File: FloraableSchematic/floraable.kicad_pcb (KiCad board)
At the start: 2 copper layers, 27 parts, among them J1 USB_B, J2 soil moisture sensor, J3 water pump, Q1 IRL1404Z, Q2 IRL1404Z, U1 BA33BC0T, U2 BH1750, U3 NodeMCU, U4 TEM-HUM-AM2302(4P-25.0X15.0MM)

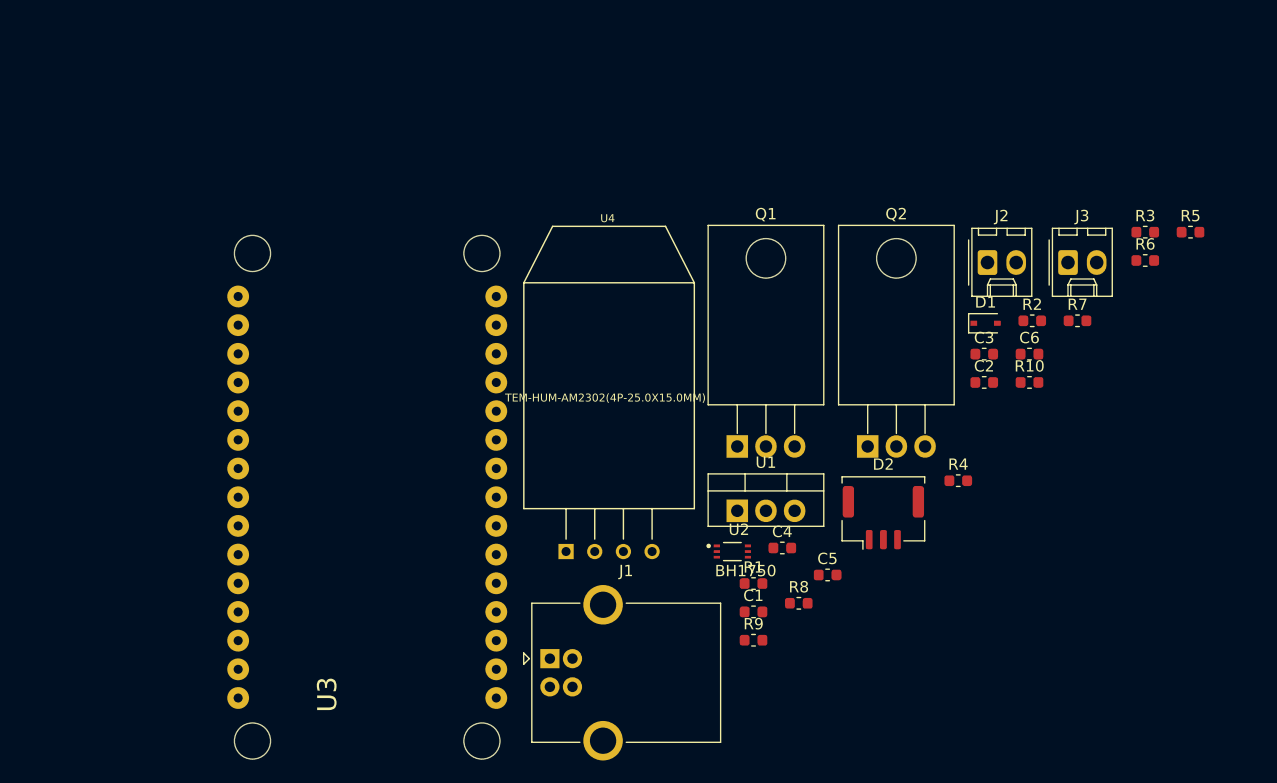
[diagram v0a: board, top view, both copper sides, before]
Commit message: check for existing devices
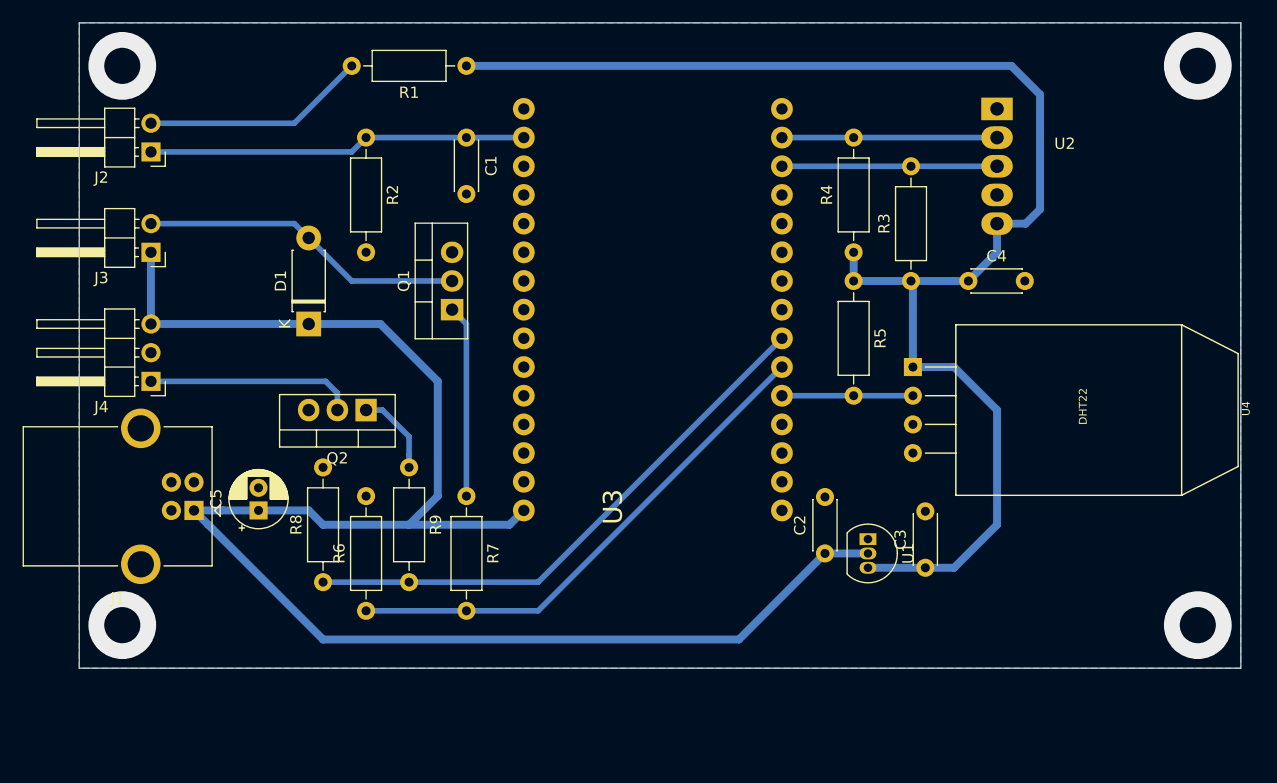
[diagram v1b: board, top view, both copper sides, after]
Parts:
- removed the C3 at (185.6, 94.1)
- removed D2: LED strip, Connector_Molex:Molex_CLIK-Mate_502382-0370_1x03-1MP_P1.25mm_Vertical
- removed the R3 at (199.8, 83.3)
- added J4: LED strip, Connector_PinHeader_2.54mm:PinHeader_1x03_P2.54mm_Horizontal, F.Cu at (111.8, 96.5)
- C1: footprint Capacitor_SMD:C_0603_1608Metric -> Capacitor_THT:C_Disc_D4.3mm_W1.9mm_P5.00mm
- C2: value 0.33u -> 1u; footprint Capacitor_SMD:C_0603_1608Metric -> Capacitor_THT:C_Disc_D4.3mm_W1.9mm_P5.00mm
- C3: renamed from C4; value 100u -> 1u; footprint Capacitor_SMD:C_0603_1608Metric -> Capacitor_THT:C_Disc_D4.3mm_W1.9mm_P5.00mm
- C4: renamed from C6; footprint Capacitor_SMD:C_0603_1608Metric -> Capacitor_THT:C_Disc_D4.3mm_W1.9mm_P5.00mm
- C5: value 100n -> 100u; footprint Capacitor_SMD:C_0603_1608Metric -> Capacitor_THT:CP_Radial_D5.0mm_P2.00mm
- D1: footprint Diode_SMD:D_SOD-323 -> Diode_THT:D_DO-41_SOD81_P7.62mm_Horizontal
- J2, J3: footprint Connector_Molex:Molex_KK-254_AE-6410-02A_1x02_P2.54mm_Vertical -> Connector_PinHeader_2.54mm:PinHeader_1x02_P2.54mm_Horizontal
- Q1, Q2: footprint Package_TO_SOT_THT:TO-220-3_Horizontal_TabDown -> Package_TO_SOT_THT:TO-220-3_Vertical
- R1, R2: footprint Resistor_SMD:R_0603_1608Metric -> Resistor_THT:R_Axial_DIN0207_L6.3mm_D2.5mm_P10.16mm_Horizontal
- R3: renamed from R4; footprint Resistor_SMD:R_0603_1608Metric -> Resistor_THT:R_Axial_DIN0207_L6.3mm_D2.5mm_P10.16mm_Horizontal
- R4: renamed from R5; footprint Resistor_SMD:R_0603_1608Metric -> Resistor_THT:R_Axial_DIN0207_L6.3mm_D2.5mm_P10.16mm_Horizontal
- R5: renamed from R6; footprint Resistor_SMD:R_0603_1608Metric -> Resistor_THT:R_Axial_DIN0207_L6.3mm_D2.5mm_P10.16mm_Horizontal
- R6: renamed from R7; footprint Resistor_SMD:R_0603_1608Metric -> Resistor_THT:R_Axial_DIN0207_L6.3mm_D2.5mm_P10.16mm_Horizontal
- R7: renamed from R8; footprint Resistor_SMD:R_0603_1608Metric -> Resistor_THT:R_Axial_DIN0207_L6.3mm_D2.5mm_P10.16mm_Horizontal
- R8: renamed from R9; footprint Resistor_SMD:R_0603_1608Metric -> Resistor_THT:R_Axial_DIN0207_L6.3mm_D2.5mm_P10.16mm_Horizontal
- R9: renamed from R10; footprint Resistor_SMD:R_0603_1608Metric -> Resistor_THT:R_Axial_DIN0207_L6.3mm_D2.5mm_P10.16mm_Horizontal
- U1: value BA33BC0T -> MCP1702-3302E/TO; footprint Package_TO_SOT_THT:TO-220-3_Vertical -> Package_TO_SOT_THT:TO-92_Inline
- U2: value BH1750 -> BH1750_module; footprint BH1750FVI-TR:XDCR_BH1750FVI-TR -> floraable:BH1750_module
- U3: footprint ESP12E_DEVKIT:ESP12E_DEVKIT -> floraable:newNodeMCU
- U4: value TEM-HUM-AM2302(4P-25.0X15.0MM) -> DHT22
- moved J3 81.2 mm to (111.8, 85.1), turned to 180 degrees
- moved J2 74.7 mm to (111.8, 76.2), turned to 180 degrees
- moved R6 68.0 mm to (130.8, 116.8), turned to 90 degrees
- moved R2 61.2 mm to (130.8, 74.9), turned to 270 degrees
- moved D1 59.9 mm to (125.7, 91.4), turned to 90 degrees
- moved R9 55.5 mm to (134.6, 104.1), turned to 270 degrees
- moved R1 52.4 mm to (139.7, 68.6), turned to 180 degrees
- moved C5 50.7 mm to (121.3, 108.0), turned to 90 degrees
- moved C1 49.1 mm to (139.7, 74.9), turned to 270 degrees
- moved Q2 44.5 mm to (130.8, 99.1), turned to 180 degrees
- moved U2 41.4 mm to (186.7, 77.5)
- moved U4 40.7 mm to (193.0, 99.1), turned to 270 degrees
- moved R8 38.5 mm to (127.0, 114.3), turned to 90 degrees
- moved J1 34.1 mm to (115.6, 108.0), turned to 180 degrees
- moved R7 30.9 mm to (139.7, 106.7), turned to 270 degrees
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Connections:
- C5 pad 1: Net-(C5-Pad1) -> +5V
- J2 pad 1: Net-(J2-Pad1) -> SOIL
- J2 pad 2: SOIL -> Net-(J2-Pad2)
- R1 pad 2: Net-(J2-Pad1) -> Net-(J2-Pad2)
- U1 pad 1: +5V -> GND
- U1 pad 2: GND -> +5V
- U2 pad 1: +3V3 -> Net-(U2-Pad1)
- U2 pad 2: Net-(U2-Pad2) -> SDA
- U2 pad 3: GND -> SCL
- U2 pad 4: SDA -> GND
- U2 pad 5: Net-(C5-Pad1) -> +3V3
- U3 pad D3: TEMPERATURE -> Net-(U3-PadD3)
- U3 pad D8: Net-(U3-PadD8) -> TEMPERATURE
- U3 pad GND@0: Net-(U3-PadGND@0) -> GND
- U3 pad GND@2: Net-(U3-PadGND@2) -> GND
- U3 pad GND@3: Net-(U3-PadGND@3) -> GND
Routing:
- net +5V: track 0.00 -> 145.4 mm
- net +3V3: track 0.00 -> 125.1 mm
- net LEDSTRIP: track 0.00 -> 49.6 mm
- net PUMP: track 0.00 -> 45.8 mm
- net SOIL: track 0.00 -> 33.5 mm
- net Net-(D1-Pad2): track 0.00 -> 28.8 mm
- net Net-(J2-Pad2): track 0.00 -> 19.9 mm
- net SDA: track 0.00 -> 19.1 mm
- net SCL: track 0.00 -> 19.1 mm
- net Net-(J4-Pad1): track 0.00 -> 18.4 mm
- net Net-(Q1-Pad1): track 0.00 -> 17.0 mm
- net TEMPERATURE: track 0.00 -> 11.6 mm
- net Net-(Q2-Pad1): track 0.00 -> 7.51 mm
- net (no net): vias 0 -> 4
- added copper zone on B.Cu, net GND
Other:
- board outline added: 102.9 x 57.2 mm
- rule trace_min: 0.2 -> 0.254
- rule via_min_size: 0.4 -> 0.508

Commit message: Add files via upload
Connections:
- U3 pad D5: Net-(U3-PadD5) -> TEMPERATURE
- U3 pad D8: TEMPERATURE -> Net-(U3-PadD8)
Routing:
- net TEMPERATURE: track 11.6 -> 17.0 mm
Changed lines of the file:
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@@
     (thickness 1.6)
     (drawings 6)
-    (tracks 69)
+    (tracks 71)
     (zones 0)
     (modules 25)
@@
     (40 Dwgs.User user)
     (41 Cmts.User user)
-    (42 Eco1.User user)
+    (42 Eco1.User user hide)
     (43 Eco2.User user)
     (44 Edge.Cuts user)
@@
   )
   (setup
-    (last_trace_width 0.7)
+    (last_trace_width 0.25)
     (user_trace_width 0.3)
     (user_trace_width 0.5)
@@
   (net 29 "Net-(U3-PadD4)")
   (net 30 "Net-(U3-Pad3V3@1)")
-  (net 31 "Net-(U3-PadD5)")
-  (net 32 PUMP)
-  (net 33 "Net-(U3-PadRX)")
-  (net 34 "Net-(U3-PadTX)")
-  (net 35 "Net-(U3-Pad3V3@2)")
-  (net 36 "Net-(U4-PadP$3)")
-  (net 37 "Net-(J2-Pad2)")
-  (net 38 "Net-(J4-Pad1)")
+  (net 31 PUMP)
+  (net 32 "Net-(U3-PadRX)")
+  (net 33 "Net-(U3-PadTX)")
+  (net 34 "Net-(U3-Pad3V3@2)")
+  (net 35 "Net-(U4-PadP$3)")
+  (net 36 "Net-(J2-Pad2)")
+  (net 37 "Net-(J4-Pad1)")
+  (net 38 "Net-(U3-PadD8)")
   (net_class Default "This is the default net class."
     (clearance 0.2)
@@
     (add_net "Net-(U3-PadD3)")
     (add_net "Net-(U3-PadD4)")
-    (add_net "Net-(U3-PadD5)")
+    (add_net "Net-(U3-PadD8)")
     (add_net "Net-(U3-PadEN)")
     (add_net "Net-(U3-PadRST)")
@@
     (fp_line (start -12.7 24.13) (end -12.7 -24.13) (layer F.Fab) (width 0.2032))
     (pad 3V3@2 thru_hole circle (at 11.43 17.78) (size 1.9304 1.9304) (drill 1) (layers *.Cu *.Mask)
-      (net 35 "Net-(U3-Pad3V3@2)") (solder_mask_margin 0.1016))
+      (net 34 "Net-(U3-Pad3V3@2)") (solder_mask_margin 0.1016))
     (pad GND@3 thru_hole circle (at 11.43 15.24) (size 1.9304 1.9304) (drill 1) (layers *.Cu *.Mask)
       (net 2 GND) (solder_mask_margin 0.1016))
     (pad TX thru_hole circle (at 11.43 12.7) (size 1.9304 1.9304) (drill 1) (layers *.Cu *.Mask)
-      (net 34 "Net-(U3-PadTX)") (solder_mask_margin 0.1016))
+      (net 33 "Net-(U3-PadTX)") (solder_mask_margin 0.1016))
     (pad RX thru_hole circle (at 11.43 10.16) (size 1.9304 1.9304) (drill 1) (layers *.Cu *.Mask)
-      (net 33 "Net-(U3-PadRX)") (solder_mask_margin 0.1016))
+      (net 32 "Net-(U3-PadRX)") (solder_mask_margin 0.1016))
     (pad D8 thru_hole circle (at 11.43 7.62) (size 1.9304 1.9304) (drill 1) (layers *.Cu *.Mask)
-      (net 10 TEMPERATURE) (solder_mask_margin 0.1016))
+      (net 38 "Net-(U3-PadD8)") (solder_mask_margin 0.1016))
     (pad D7 thru_hole circle (at 11.43 5.08) (size 1.9304 1.9304) (drill 1) (layers *.Cu *.Mask)
-      (net 32 PUMP) (solder_mask_margin 0.1016))
+      (net 31 PUMP) (solder_mask_margin 0.1016))
     (pad D6 thru_hole circle (at 11.43 2.54) (size 1.9304 1.9304) (drill 1) (layers *.Cu *.Mask)
       (net 11 LEDSTRIP) (solder_mask_margin 0.1016))
     (pad D5 thru_hole circle (at 11.43 0) (size 1.9304 1.9304) (drill 1) (layers *.Cu *.Mask)
-      (net 31 "Net-(U3-PadD5)") (solder_mask_margin 0.1016))
+      (net 10 TEMPERATURE) (solder_mask_margin 0.1016))
     (pad GND@2 thru_hole circle (at 11.43 -2.54) (size 1.9304 1.9304) (drill 1) (layers *.Cu *.Mask)
       (net 2 GND) (solder_mask_margin 0.1016))
@@
       (net 2 GND))
     (pad 2 thru_hole oval (at 2.54 0 180) (size 1.905 2) (drill 1.1) (layers *.Cu *.Mask)
-      (net 38 "Net-(J4-Pad1)"))
+      (net 37 "Net-(J4-Pad1)"))
     (pad 1 thru_hole rect (at 0 0 180) (size 1.905 2) (drill 1.1) (layers *.Cu *.Mask)
       (net 7 "Net-(Q2-Pad1)"))
@@
     (fp_line (start 1.93 -1.25) (end 1.93 1.25) (layer F.Fab) (width 0.1))
     (pad 2 thru_hole oval (at 10.16 0 270) (size 1.6 1.6) (drill 0.8) (layers *.Cu *.Mask)
-      (net 32 PUMP))
+      (net 31 PUMP))
     (pad 1 thru_hole circle (at 0 0 270) (size 1.6 1.6) (drill 0.8) (layers *.Cu *.Mask)
       (net 6 "Net-(Q1-Pad1)"))
@@
       (net 2 GND))
     (pad 1 thru_hole circle (at 0 0 90) (size 1.6 1.6) (drill 0.8) (layers *.Cu *.Mask)
-      (net 32 PUMP))
+      (net 31 PUMP))
     (model ${KISYS3DMOD}/Resistor_THT.3dshapes/R_Axial_DIN0207_L6.3mm_D2.5mm_P10.16mm_Horizontal.wrl
       (at (xyz 0 0 0))
@@
     (fp_line (start 1.93 -1.25) (end 1.93 1.25) (layer F.Fab) (width 0.1))
     (pad 2 thru_hole oval (at 10.16 0 180) (size 1.6 1.6) (drill 0.8) (layers *.Cu *.Mask)
-      (net 37 "Net-(J2-Pad2)"))
+      (net 36 "Net-(J2-Pad2)"))
     (pad 1 thru_hole circle (at 0 0 180) (size 1.6 1.6) (drill 0.8) (layers *.Cu *.Mask)
       (net 4 +3V3))
@@
     (fp_line (start 2.135 -1.27) (end 4.04 -1.27) (layer F.Fab) (width 0.1))
     (pad 2 thru_hole oval (at 0 2.54 180) (size 1.7 1.7) (drill 1) (layers *.Cu *.Mask)
-      (net 37 "Net-(J2-Pad2)"))
+      (net 36 "Net-(J2-Pad2)"))
     (pad 1 thru_hole rect (at 0 0 180) (size 1.7 1.7) (drill 1) (layers *.Cu *.Mask)
       (net 1 SOIL))
@@
       (net 2 GND))
     (pad P$3 thru_hole circle (at 1.27 13.8 270) (size 1.6 1.6) (drill 0.8) (layers *.Cu *.Mask)
-      (net 36 "Net-(U4-PadP$3)"))
+      (net 35 "Net-(U4-PadP$3)"))
     (pad P$2 thru_hole circle (at -1.27 13.8 270) (size 1.6 1.6) (drill 0.8) (layers *.Cu *.Mask)
       (net 10 TEMPERATURE))
@@
       (net 14 "Net-(J4-Pad2)"))
     (pad 1 thru_hole rect (at 0 0 180) (size 1.7 1.7) (drill 1) (layers *.Cu *.Mask)
-      (net 38 "Net-(J4-Pad1)"))
+      (net 37 "Net-(J4-Pad1)"))
     (model "D:/folder 0/download/KiCad/lib/DS1070-RA (WF-RA CONNFLY)/DS1070-3MR (WF-3RA CONNFLY).stp"
       (at (xyz 0 0 0))
@@
   (segment (start 173.99 74.93) (end 167.64 74.93) (width 0.5) (layer B.Cu) (net 9))
   (segment (start 179.24 97.79) (end 173.99 97.79) (width 0.5) (layer B.Cu) (net 10))
-  (segment (start 173.99 97.79) (end 167.64 97.79) (width 0.5) (layer B.Cu) (net 10))
+  (segment (start 170.18 90.17) (end 167.64 90.17) (width 0.5) (layer B.Cu) (net 10))
+  (segment (start 173.99 97.79) (end 173.99 93.98) (width 0.5) (layer B.Cu) (net 10))
+  (segment (start 173.99 93.98) (end 170.18 90.17) (width 0.5) (layer B.Cu) (net 10))
   (segment (start 146.05 114.3) (end 167.64 92.71) (width 0.5) (layer B.Cu) (net 11))
   (segment (start 134.62 114.3) (end 146.05 114.3) (width 0.5) (layer B.Cu) (net 11))
   (segment (start 127 114.3) (end 134.62 114.3) (width 0.5) (layer B.Cu) (net 11))
-  (segment (start 139.7 116.84) (end 146.05 116.84) (width 0.5) (layer B.Cu) (net 32))
-  (segment (start 146.05 116.84) (end 167.64 95.25) (width 0.5) (layer B.Cu) (net 32))
-  (segment (start 130.81 116.84) (end 139.7 116.84) (width 0.5) (layer B.Cu) (net 32))
-  (segment (start 124.46 73.66) (end 129.54 68.58) (width 0.5) (layer B.Cu) (net 37))
-  (segment (start 111.76 73.66) (end 124.46 73.66) (width 0.5) (layer B.Cu) (net 37))
-  (segment (start 128.27 97.56) (end 128.27 99.06) (width 0.5) (layer B.Cu) (net 38))
-  (segment (start 111.76 96.52) (end 127.23 96.52) (width 0.5) (layer B.Cu) (net 38))
-  (segment (start 127.23 96.52) (end 128.27 97.56) (width 0.5) (layer B.Cu) (net 38))
+  (segment (start 139.7 116.84) (end 146.05 116.84) (width 0.5) (layer B.Cu) (net 31))
+  (segment (start 146.05 116.84) (end 167.64 95.25) (width 0.5) (layer B.Cu) (net 31))
+  (segment (start 130.81 116.84) (end 139.7 116.84) (width 0.5) (layer B.Cu) (net 31))
+  (segment (start 124.46 73.66) (end 129.54 68.58) (width 0.5) (layer B.Cu) (net 36))
+  (segment (start 111.76 73.66) (end 124.46 73.66) (width 0.5) (layer B.Cu) (net 36))
+  (segment (start 128.27 97.56) (end 128.27 99.06) (width 0.5) (layer B.Cu) (net 37))
+  (segment (start 111.76 96.52) (end 127.23 96.52) (width 0.5) (layer B.Cu) (net 37))
+  (segment (start 127.23 96.52) (end 128.27 97.56) (width 0.5) (layer B.Cu) (net 37))
   (zone (net 2) (net_name GND) (layer B.Cu) (hatch edge 0.508)
     (connect_pads (clearance 0.508))
     (min_thickness 0.254)
-    (fill yes (arc_segments 32) (thermal_gap 0.508) (thermal_bridge_width 0.508))
+    (fill (arc_segments 32) (thermal_gap 0.508) (thermal_bridge_width 0.508))
     (polygon
       (pts
